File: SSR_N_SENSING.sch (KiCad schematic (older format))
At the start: 16 parts, among them P2 CONN_01X02, Q1 BC850, U2 ACS722

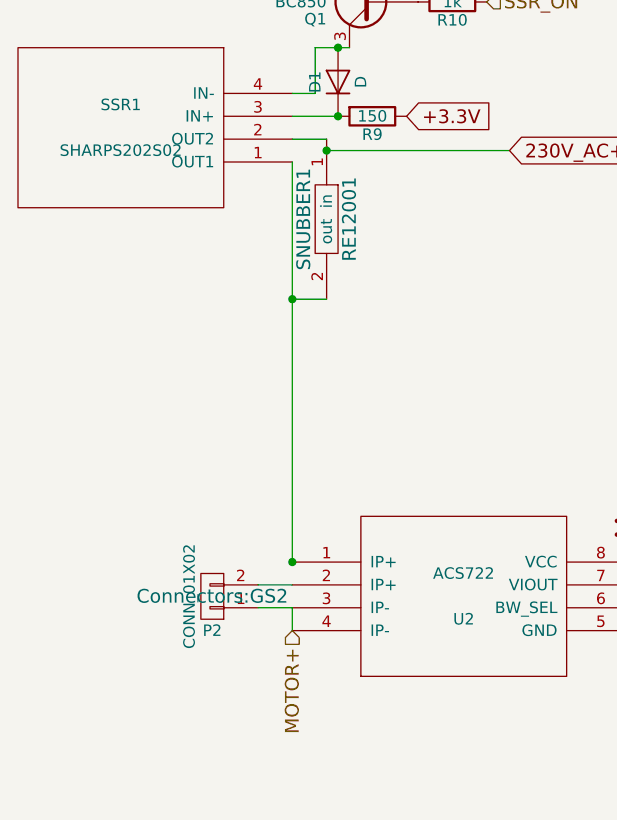
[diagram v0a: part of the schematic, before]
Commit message: backup before rewiring.
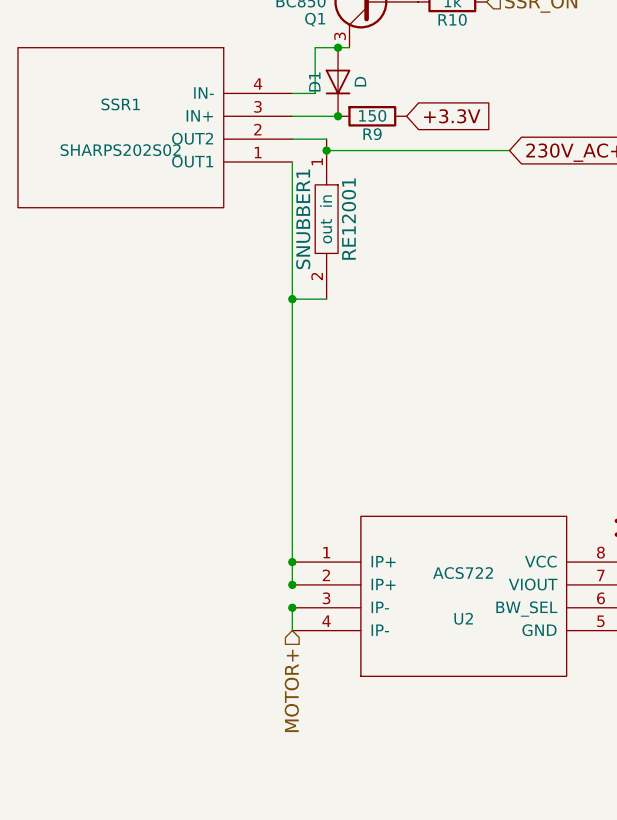
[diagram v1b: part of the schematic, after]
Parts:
- removed P2: CONN_01X02, Connectors:GS2, symbol CONN_01X02
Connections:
- net at SNUBBER1.2 (out), SSR1.1 (OUT1), U2.1 (IP+): now also U2.2 (IP+)
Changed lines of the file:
@@
 	1    0    0    -1
-$EndComp
-$Comp
-L CONN_01X02 P2
-U 1 1 5626DE5E
-P 3100 4400
-F 0 "P2" H 3100 4550 50  0000 C CNN
-F 1 "CONN_01X02" V 3200 4400 50  0000 C CNN
-F 2 "Connectors:GS2" H 3100 4400 60  0000 C CNN
-F 3 "" H 3100 4400 60  0000 C CNN
-	1    3100 4400
-	-1   0    0    1
 $EndComp
 Wire Wire Line
@@
 Wire Wire Line
 	6100 4700 6100 4750
-Wire Wire Line
-	3450 4350 3300 4350
-Wire Wire Line
-	3300 4450 3450 4450
 Connection ~ 3650 2000
 Wire Wire Line
-	3450 4250 3450 2500
+	3450 2500 3450 4350
 Wire Wire Line
 	4950 4250 5450 4250
@@
 	3600 2450 4400 2450
 Connection ~ 3600 2450
+Connection ~ 3450 4350
+Connection ~ 3450 4450
 $EndSCHEMATC

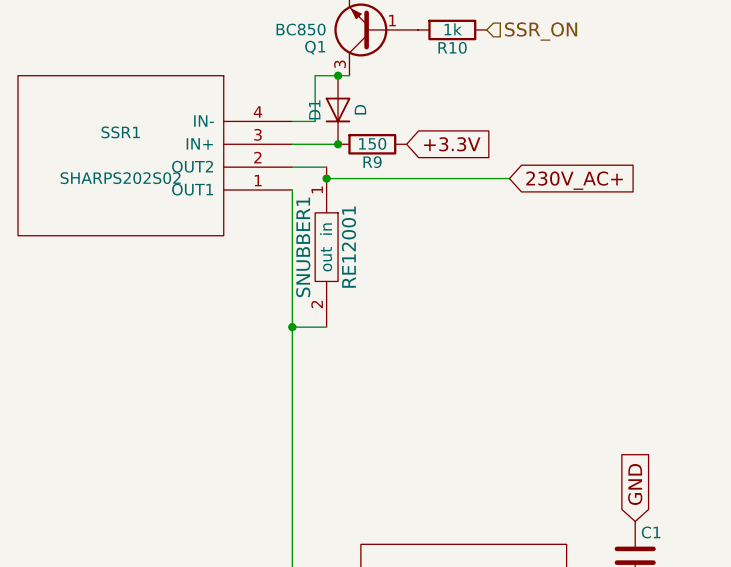
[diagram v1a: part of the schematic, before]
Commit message: this version has the parts organized; before routing
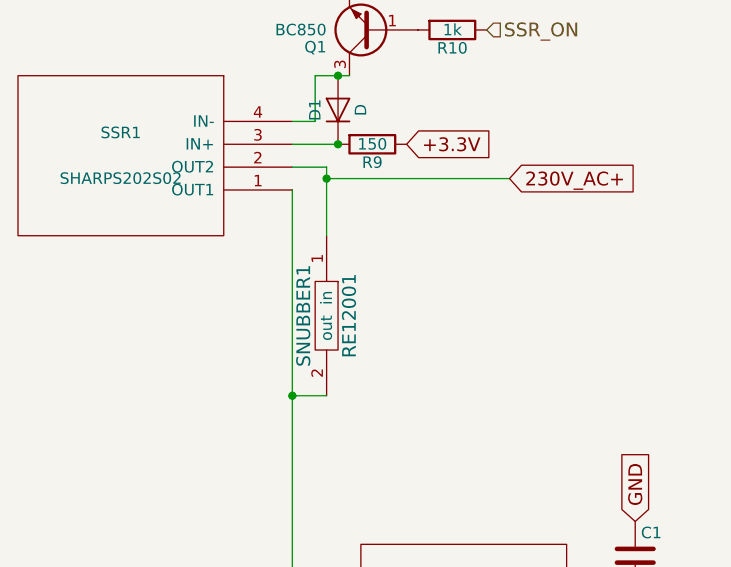
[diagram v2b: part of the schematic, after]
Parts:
- D1, D2: footprint Diodes_SMD:D_SMC_Handsoldering -> Diodes_SMD:D_SMA_Handsoldering
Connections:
- net 230V_AC+: now also SNUBBER1.1 (in), SSR1.2 (OUT2)
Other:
- moved on the sheet: SNUBBER1
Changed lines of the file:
@@
 F 0 "D1" H 3650 2250 50  0000 C CNN
 F 1 "D" H 3650 2050 50  0000 C CNN
-F 2 "Diodes_SMD:D_SMC_Handsoldering" H 3650 2150 60  0001 C CNN
+F 2 "Diodes_SMD:D_SMA_Handsoldering" H 3650 2150 60  0001 C CNN
 F 3 "http://hu.farnell.com/on-semiconductor/mbra2h100t3g/schottky-rect-2a-100v-sma/dp/2533233" H 3650 2150 60  0001 C CNN
 	1    3650 2150
@@
 F 0 "D2" H 6100 5000 50  0000 C CNN
 F 1 "D" H 6100 4800 50  0000 C CNN
-F 2 "Diodes_SMD:D_SMC_Handsoldering" H 6100 4900 60  0001 C CNN
+F 2 "Diodes_SMD:D_SMA_Handsoldering" H 6100 4900 60  0001 C CNN
 F 3 "http://hu.farnell.com/on-semiconductor/mbra2h100t3g/schottky-rect-2a-100v-sma/dp/2533233" H 6100 4900 60  0001 C CNN
 	1    6100 4900
@@
 L RE12001 SNUBBER1
 U 1 1 592C0F5A
-P 3600 2750
-F 0 "SNUBBER1" H 3600 2650 60  0000 C CNN
-F 1 "RE12001" H 3600 2850 60  0000 C CNN
-F 2 "water:RE12001" H 3600 2850 60  0001 C CNN
-F 3 "http://hu.farnell.com/roxburgh/re12001/rc-network-250v-0-01uf-120r-pcb/dp/2336106" H 3600 2850 60  0001 C CNN
-	1    3600 2750
+P 3600 3050
+F 0 "SNUBBER1" H 3600 2950 60  0000 C CNN
+F 1 "RE12001" H 3600 3150 60  0000 C CNN
+F 2 "water:RE12001" H 3600 3150 60  0001 C CNN
+F 3 "http://hu.farnell.com/roxburgh/re12001/rc-network-250v-0-01uf-120r-pcb/dp/2336106" H 3600 3150 60  0001 C CNN
+	1    3600 3050
 	0    1    1    0
 $EndComp
@@
 Wire Wire Line
 	3450 2400 3600 2400
-Wire Wire Line
-	3450 3100 3600 3100
-Connection ~ 3450 3100
 Wire Wire Line
 	3600 2450 4400 2450
@@
 Connection ~ 3450 4350
 Connection ~ 3450 4450
+Wire Wire Line
+	3600 3400 3450 3400
+Connection ~ 3450 3400
+Wire Wire Line
+	3600 2400 3600 2700
 $EndSCHEMATC

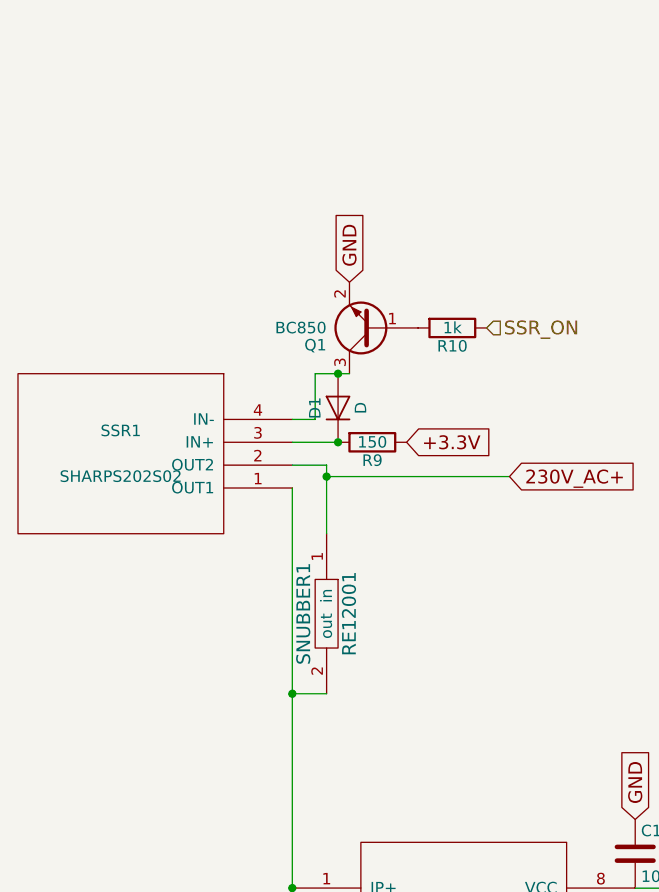
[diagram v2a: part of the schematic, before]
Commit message: fixed links to the webpage of parts
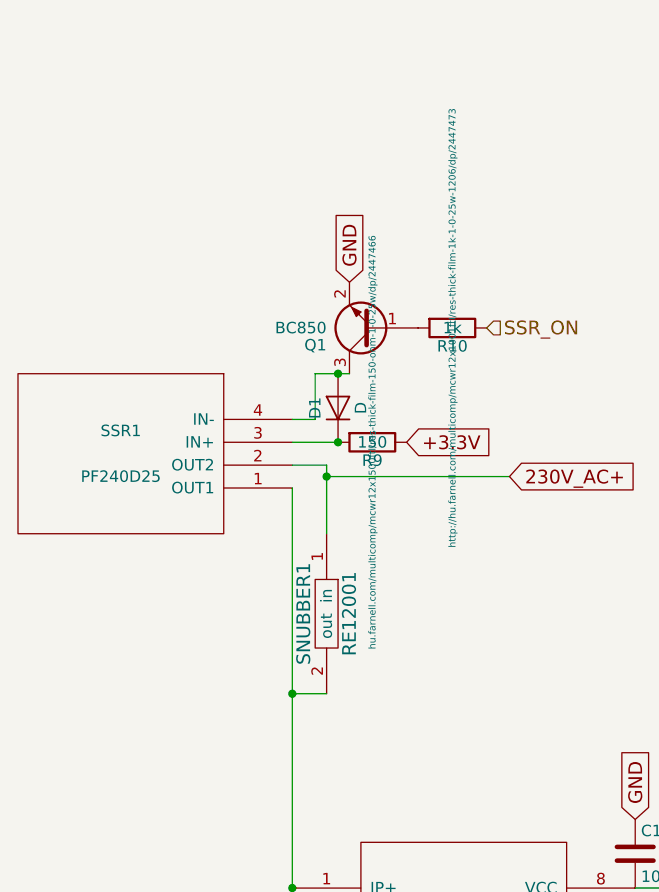
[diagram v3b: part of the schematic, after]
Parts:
- SNUBBER1: alternative (none) -> http://hu.farnell.com/roxburgh/re1201/rc-network-250v-0-1uf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
- SSR1: value SHARPS202S02 -> PF240D25
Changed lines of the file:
@@
 P 2700 2350
 F 0 "SSR1" H 2700 2250 50  0000 C CNN
-F 1 "SHARPS202S02" H 2700 2450 50  0000 C CNN
+F 1 "PF240D25" H 2700 2450 50  0000 C CNN
 F 2 "water:s202s02" H 2700 2350 50  0001 C CNN
-F 3 "https://www.digikey.com/product-detail/en/sharp-microelectronics/S202S02/425-1246-5-ND/458265" H 2700 2350 50  0001 C CNN
+F 3 "http://hu.farnell.com/crydom/pf240d25/ssr-3-15vdc-12-280vac-25a/dp/1200285" H 2700 2350 50  0001 C CNN
 F 4 "https://www.hestore.hu/prod_10023091.html" H 2700 2350 60  0001 C CNN "Store"
 	1    2700 2350
@@
 F 1 "150" V 3800 2300 50  0000 C CNN
 F 2 "Resistors_SMD:R_1206_HandSoldering" V 3730 2300 30  0001 C CNN
-F 3 "" H 3800 2300 30  0000 C CNN
+F 3 "hu.farnell.com/multicomp/mcwr12x1500ftl/res-thick-film-150-ohm-1-0-25w/dp/2447466" H 3800 2300 30  0000 C CNN
 	1    3800 2300
 	0    1    1    0
@@
 F 1 "1k" V 4150 1800 50  0000 C CNN
 F 2 "Resistors_SMD:R_1206_HandSoldering" V 4080 1800 30  0001 C CNN
-F 3 "" H 4150 1800 30  0000 C CNN
+F 3 "http://hu.farnell.com/multicomp/mcwr12x1001ftl/res-thick-film-1k-1-0-25w-1206/dp/2447473" H 4150 1800 30  0000 C CNN
 	1    4150 1800
 	0    1    1    0
@@
 F 1 "10uF" H 4975 4000 50  0000 L CNN
 F 2 "Capacitors_SMD:C_1206_HandSoldering" H 4988 3950 30  0001 C CNN
-F 3 "" H 4950 4100 60  0000 C CNN
+F 3 "http://hu.farnell.com/vishay/vj1206y106kxxtw1bc/cap-mlcc-x7r-10uf-25v-1206/dp/2407348" H 4950 4100 60  0001 C CNN
 	1    4950 4100
 	1    0    0    -1
@@
 F 1 "100k" V 6200 5200 50  0000 C CNN
 F 2 "Resistors_SMD:R_1206_HandSoldering" V 6130 5200 30  0001 C CNN
-F 3 "" H 6200 5200 30  0000 C CNN
+F 3 "http://hu.farnell.com/vishay/crcw1206100kfkea/res-thick-film-100k-1-0-25w-1206/dp/1469975" H 6200 5200 30  0001 C CNN
 	1    6200 5200
 	-1   0    0    1
@@
 F 1 "1nF" H 5175 4500 50  0000 L CNN
 F 2 "Capacitors_SMD:C_1206_HandSoldering" H 5188 4450 30  0001 C CNN
-F 3 "" H 5150 4600 60  0000 C CNN
+F 3 "http://hu.farnell.com/vishay/vj1206y102kxeac/cap-mlcc-x7r-1000pf-500v-1206/dp/2407307" H 5150 4600 60  0001 C CNN
 	1    5150 4600
 	1    0    0    -1
@@
 F 1 "3k" V 5700 4900 50  0000 C CNN
 F 2 "Resistors_SMD:R_1206_HandSoldering" V 5630 4900 30  0001 C CNN
-F 3 "" H 5700 4900 30  0000 C CNN
+F 3 "http://hu.farnell.com/vishay/crcw12063k00fkea/res-thick-film-3k-1-0-25w-1206/dp/1653121" H 5700 4900 30  0001 C CNN
 	1    5700 4900
 	1    0    0    -1
@@
 F 2 "water:RE12001" H 3600 3150 60  0001 C CNN
 F 3 "http://hu.farnell.com/roxburgh/re12001/rc-network-250v-0-01uf-120r-pcb/dp/2336106" H 3600 3150 60  0001 C CNN
+F 4 "http://hu.farnell.com/roxburgh/re1201/rc-network-250v-0-1uf-120r-pcb/dp/2336109" H 3600 3050 60  0001 C CNN "alternative"
 	1    3600 3050
 	0    1    1    0

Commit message: updated links
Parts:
- SSR1: cheap alternative (none) -> http://hu.farnell.com/crydom/ed24c5/ssr-plug-in-280vac-5a-1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
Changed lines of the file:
@@
 F 3 "http://hu.farnell.com/crydom/pf240d25/ssr-3-15vdc-12-280vac-25a/dp/1200285" H 2700 2350 50  0001 C CNN
 F 4 "https://www.hestore.hu/prod_10023091.html" H 2700 2350 60  0001 C CNN "Store"
+F 5 "http://hu.farnell.com/crydom/ed24c5/ssr-plug-in-280vac-5a-18-32vdc/dp/1895444" H 2700 2350 60  0001 C CNN "cheap alternative"
 	1    2700 2350
 	-1   0    0    1

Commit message: stash commit before the revision of the parts
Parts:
- U2: 20 A alternative (none) -> http://hu.farnell.com/allegro-microsystems/acs712elctr-20a-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; 5A alternative (none) -> ACS712ELCTR-05B-T
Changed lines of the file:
@@
 F 1 "150" V 3800 2300 50  0000 C CNN
 F 2 "Resistors_SMD:R_1206_HandSoldering" V 3730 2300 30  0001 C CNN
-F 3 "hu.farnell.com/multicomp/mcwr12x1500ftl/res-thick-film-150-ohm-1-0-25w/dp/2447466" H 3800 2300 30  0000 C CNN
+F 3 "hu.farnell.com/multicomp/mcwr12x1500ftl/res-thick-film-150-ohm-1-0-25w/dp/2447466" H 3800 2300 30  0001 C CNN
 	1    3800 2300
 	0    1    1    0
@@
 F 1 "1k" V 4150 1800 50  0000 C CNN
 F 2 "Resistors_SMD:R_1206_HandSoldering" V 4080 1800 30  0001 C CNN
-F 3 "http://hu.farnell.com/multicomp/mcwr12x1001ftl/res-thick-film-1k-1-0-25w-1206/dp/2447473" H 4150 1800 30  0000 C CNN
+F 3 "http://hu.farnell.com/multicomp/mcwr12x1001ftl/res-thick-film-1k-1-0-25w-1206/dp/2447473" H 4150 1800 30  0001 C CNN
 	1    4150 1800
 	0    1    1    0
@@
 F 2 "Housings_SOIC:SOIC-8_3.9x4.9mm_Pitch1.27mm" H 4200 4400 50  0001 C CNN
 F 3 "www.allegromicro.com/~/media/Files/Datasheets/ACS722-Datasheet.ashx" H 4200 4400 50  0001 C CNN
+F 4 "http://hu.farnell.com/allegro-microsystems/acs712elctr-20a-t/sensor-current-20a-soic8/dp/1329624" H 4200 4400 60  0001 C CNN "20 A alternative"
+F 5 "ACS712ELCTR-05B-T" H 4200 4400 60  0001 C CNN "5A alternative"
 	1    4200 4400
 	1    0    0    -1

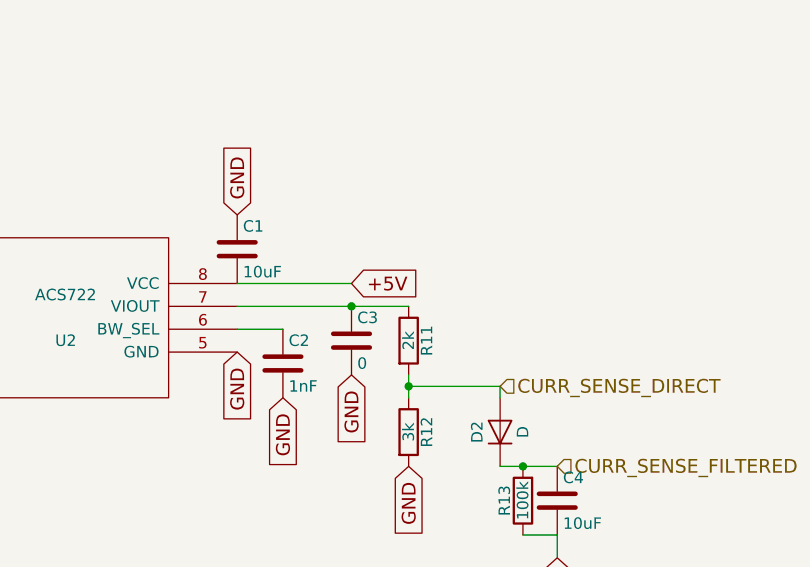
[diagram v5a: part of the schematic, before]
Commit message: parts corrected after review; dc/dc converter has to be ordered
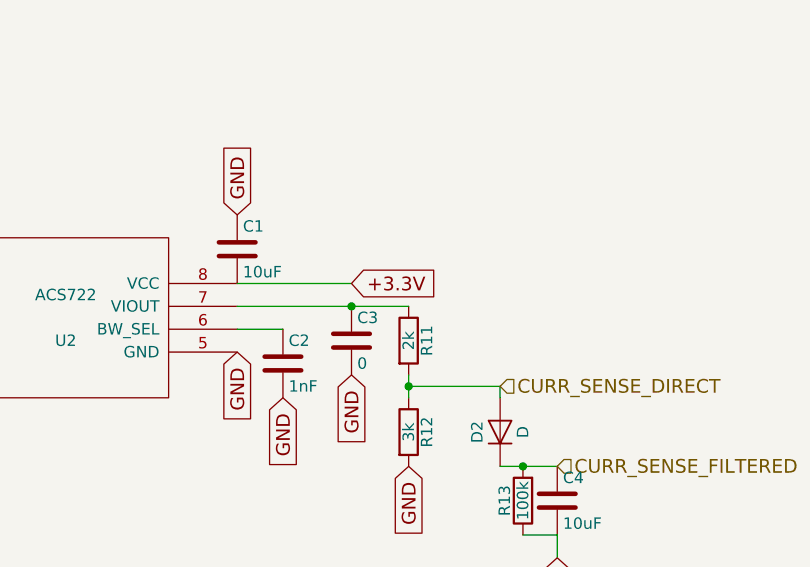
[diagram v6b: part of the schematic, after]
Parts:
- D1, D2: footprint Diodes_SMD:D_SMA_Handsoldering -> Diodes_SMD:D_SOD-123
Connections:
- net +5V is gone; now on net +3.3V: C1.2, U2.8 (VCC)
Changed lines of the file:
@@
 F 0 "D1" H 3650 2250 50  0000 C CNN
 F 1 "D" H 3650 2050 50  0000 C CNN
-F 2 "Diodes_SMD:D_SMA_Handsoldering" H 3650 2150 60  0001 C CNN
-F 3 "http://hu.farnell.com/on-semiconductor/mbra2h100t3g/schottky-rect-2a-100v-sma/dp/2533233" H 3650 2150 60  0001 C CNN
+F 2 "Diodes_SMD:D_SOD-123" H 3650 2150 60  0001 C CNN
+F 3 "http://hu.farnell.com/taiwan-semiconductor/b0540w/diode-rectif-40v-0-5a-sod123/dp/1863143" H 3650 2150 60  0001 C CNN
 	1    3650 2150
 	0    -1   -1   0
@@
 F 0 "D2" H 6100 5000 50  0000 C CNN
 F 1 "D" H 6100 4800 50  0000 C CNN
-F 2 "Diodes_SMD:D_SMA_Handsoldering" H 6100 4900 60  0001 C CNN
-F 3 "http://hu.farnell.com/on-semiconductor/mbra2h100t3g/schottky-rect-2a-100v-sma/dp/2533233" H 6100 4900 60  0001 C CNN
+F 2 "Diodes_SMD:D_SOD-123" H 6100 4900 60  0001 C CNN
+F 3 "http://hu.farnell.com/taiwan-semiconductor/b0540w/diode-rectif-40v-0-5a-sod123/dp/1863143" H 6100 4900 60  0001 C CNN
 	1    6100 4900
 	0    -1   -1   0
@@
 	4950 4250 5450 4250
 Text GLabel 5450 4250 2    60   Input ~ 0
-+5V
++3.3V
 Text GLabel 5150 4750 3    60   Input ~ 0
 GND

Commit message: before wiring
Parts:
- renumbered C1 to C3, C2 to C4, C3 to C5, C4 to C6, U2 to U3
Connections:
- net 230V_AC+: now also SNUBBER1.2 (out), SSR1.1 (OUT1); no longer SNUBBER1.1 (in), SSR1.2 (OUT2)
- net at U3.1 (IP+), U3.2 (IP+): now also SNUBBER1.1 (in), SSR1.2 (OUT2); no longer SNUBBER1.2 (out), SSR1.1 (OUT1)
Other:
- moved on the sheet: SNUBBER1
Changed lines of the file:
@@
 	-1   0    0    1
 $EndComp
-Text GLabel 4400 2450 2    60   Input ~ 0
+Text GLabel 2950 2800 0    60   Input ~ 0
 230V_AC+
 $Comp
-L ACS722 U2
+L ACS722 U3
 U 1 1 56251027
 P 4200 4400
-F 0 "U2" H 4200 4300 50  0000 C CNN
+F 0 "U3" H 4200 4300 50  0000 C CNN
 F 1 "ACS722" H 4200 4500 50  0000 C CNN
 F 2 "Housings_SOIC:SOIC-8_3.9x4.9mm_Pitch1.27mm" H 4200 4400 50  0001 C CNN
@@
 $EndComp
 $Comp
-L C C1
+L C C3
 U 1 1 562512DC
 P 4950 4100
-F 0 "C1" H 4975 4200 50  0000 L CNN
+F 0 "C3" H 4975 4200 50  0000 L CNN
 F 1 "10uF" H 4975 4000 50  0000 L CNN
 F 2 "Capacitors_SMD:C_1206_HandSoldering" H 4988 3950 30  0001 C CNN
@@
 $EndComp
 $Comp
-L C C3
+L C C5
 U 1 1 56251583
 P 5450 4500
-F 0 "C3" H 5475 4600 50  0000 L CNN
+F 0 "C5" H 5475 4600 50  0000 L CNN
 F 1 "0" H 5475 4400 50  0000 L CNN
 F 2 "Capacitors_SMD:C_1206_HandSoldering" H 5488 4350 30  0001 C CNN
@@
 $EndComp
 $Comp
-L C C4
+L C C6
 U 1 1 562518A4
 P 6350 5200
-F 0 "C4" H 6375 5300 50  0000 L CNN
+F 0 "C6" H 6375 5300 50  0000 L CNN
 F 1 "10uF" H 6375 5100 50  0000 L CNN
 F 2 "Capacitors_SMD:C_1206_HandSoldering" H 6388 5050 30  0001 C CNN
@@
 CURR_SENSE_FILTERED
 $Comp
-L C C2
+L C C4
 U 1 1 56251AFD
 P 5150 4600
-F 0 "C2" H 5175 4700 50  0000 L CNN
+F 0 "C4" H 5175 4700 50  0000 L CNN
 F 1 "1nF" H 5175 4500 50  0000 L CNN
 F 2 "Capacitors_SMD:C_1206_HandSoldering" H 5188 4450 30  0001 C CNN
@@
 Connection ~ 3650 2000
 Wire Wire Line
-	3450 2500 3450 4350
-Wire Wire Line
 	4950 4250 5450 4250
 Text GLabel 5450 4250 2    60   Input ~ 0
@@
 L RE12001 SNUBBER1
 U 1 1 592C0F5A
-P 3600 3050
-F 0 "SNUBBER1" H 3600 2950 60  0000 C CNN
-F 1 "RE12001" H 3600 3150 60  0000 C CNN
-F 2 "water:RE12001" H 3600 3150 60  0001 C CNN
-F 3 "http://hu.farnell.com/roxburgh/re12001/rc-network-250v-0-01uf-120r-pcb/dp/2336106" H 3600 3150 60  0001 C CNN
-F 4 "http://hu.farnell.com/roxburgh/re1201/rc-network-250v-0-1uf-120r-pcb/dp/2336109" H 3600 3050 60  0001 C CNN "alternative"
-	1    3600 3050
-	0    1    1    0
+P 3150 3300
+F 0 "SNUBBER1" H 3150 3200 60  0000 C CNN
+F 1 "RE12001" H 3150 3400 60  0000 C CNN
+F 2 "water:RE12001" H 3150 3400 60  0001 C CNN
+F 3 "http://hu.farnell.com/roxburgh/re12001/rc-network-250v-0-01uf-120r-pcb/dp/2336106" H 3150 3400 60  0001 C CNN
+F 4 "http://hu.farnell.com/roxburgh/re1201/rc-network-250v-0-1uf-120r-pcb/dp/2336109" H 3150 3300 60  0001 C CNN "alternative"
+	1    3150 3300
+	0    -1   -1   0
 $EndComp
 Text GLabel 3700 1600 1    60   Input ~ 0
@@
 Wire Wire Line
 	3450 2400 3600 2400
-Wire Wire Line
-	3600 2450 4400 2450
-Connection ~ 3600 2450
 Connection ~ 3450 4350
 Connection ~ 3450 4450
 Wire Wire Line
-	3600 3400 3450 3400
-Connection ~ 3450 3400
+	3600 2400 3600 2900
 Wire Wire Line
-	3600 2400 3600 2700
+	3600 2900 3450 2900
+Wire Wire Line
+	3450 2900 3450 4350
+Wire Wire Line
+	2950 2800 3500 2800
+Wire Wire Line
+	3500 2800 3500 2500
+Wire Wire Line
+	3500 2500 3450 2500
+Wire Wire Line
+	3150 2950 3150 2800
+Connection ~ 3150 2800
+Wire Wire Line
+	3150 3650 3450 3650
+Connection ~ 3450 3650
 $EndSCHEMATC
